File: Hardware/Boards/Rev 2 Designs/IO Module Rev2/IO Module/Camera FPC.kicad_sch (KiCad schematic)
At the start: 25 parts, among them J5 Cam FPC, U23 SN65DPHY440SS

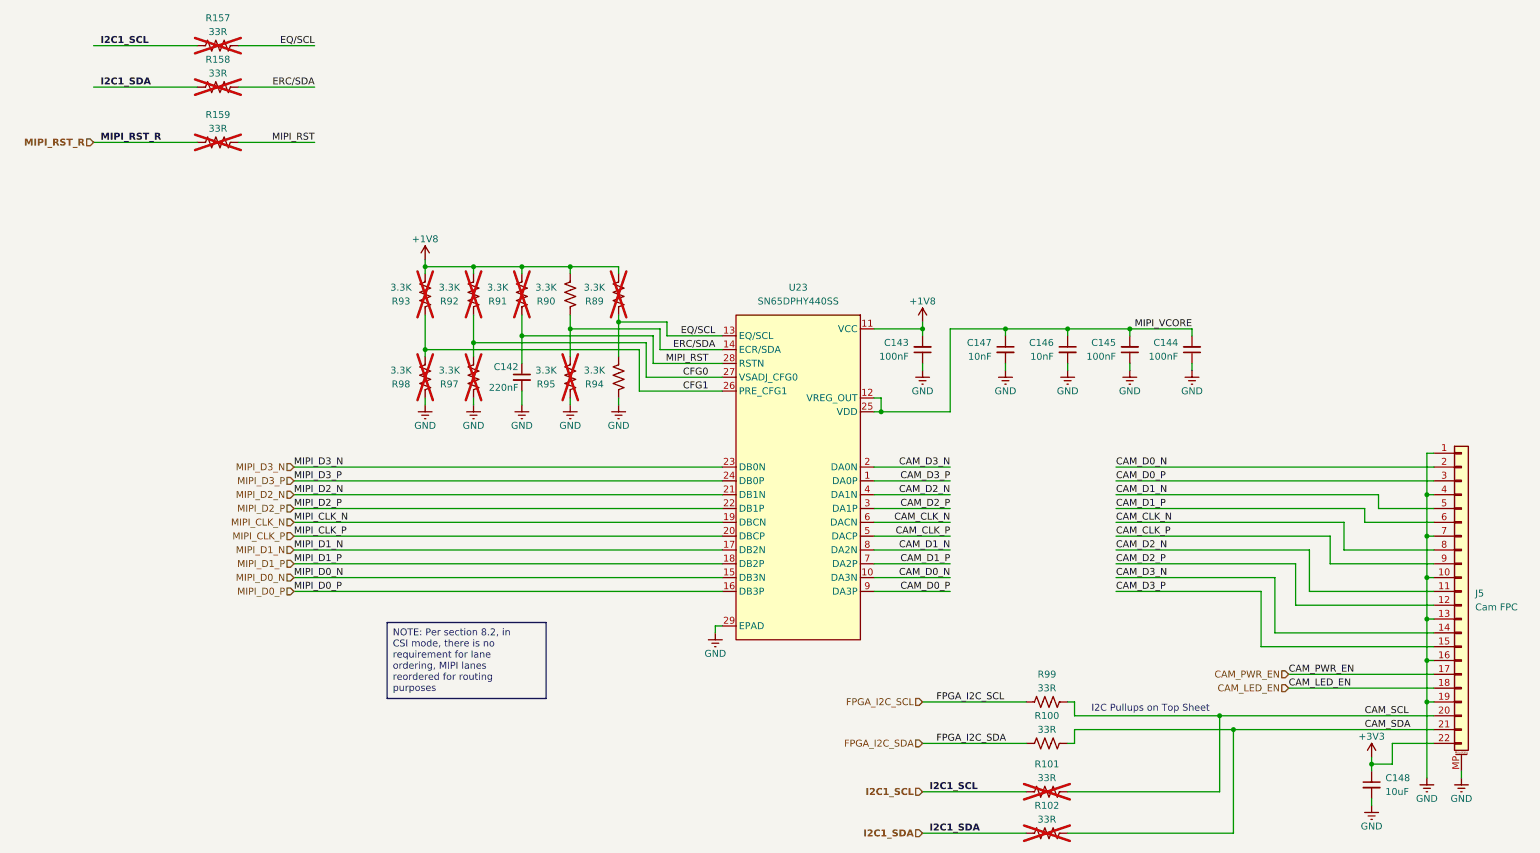
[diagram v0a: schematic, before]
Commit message: Rev 2 IO module complete
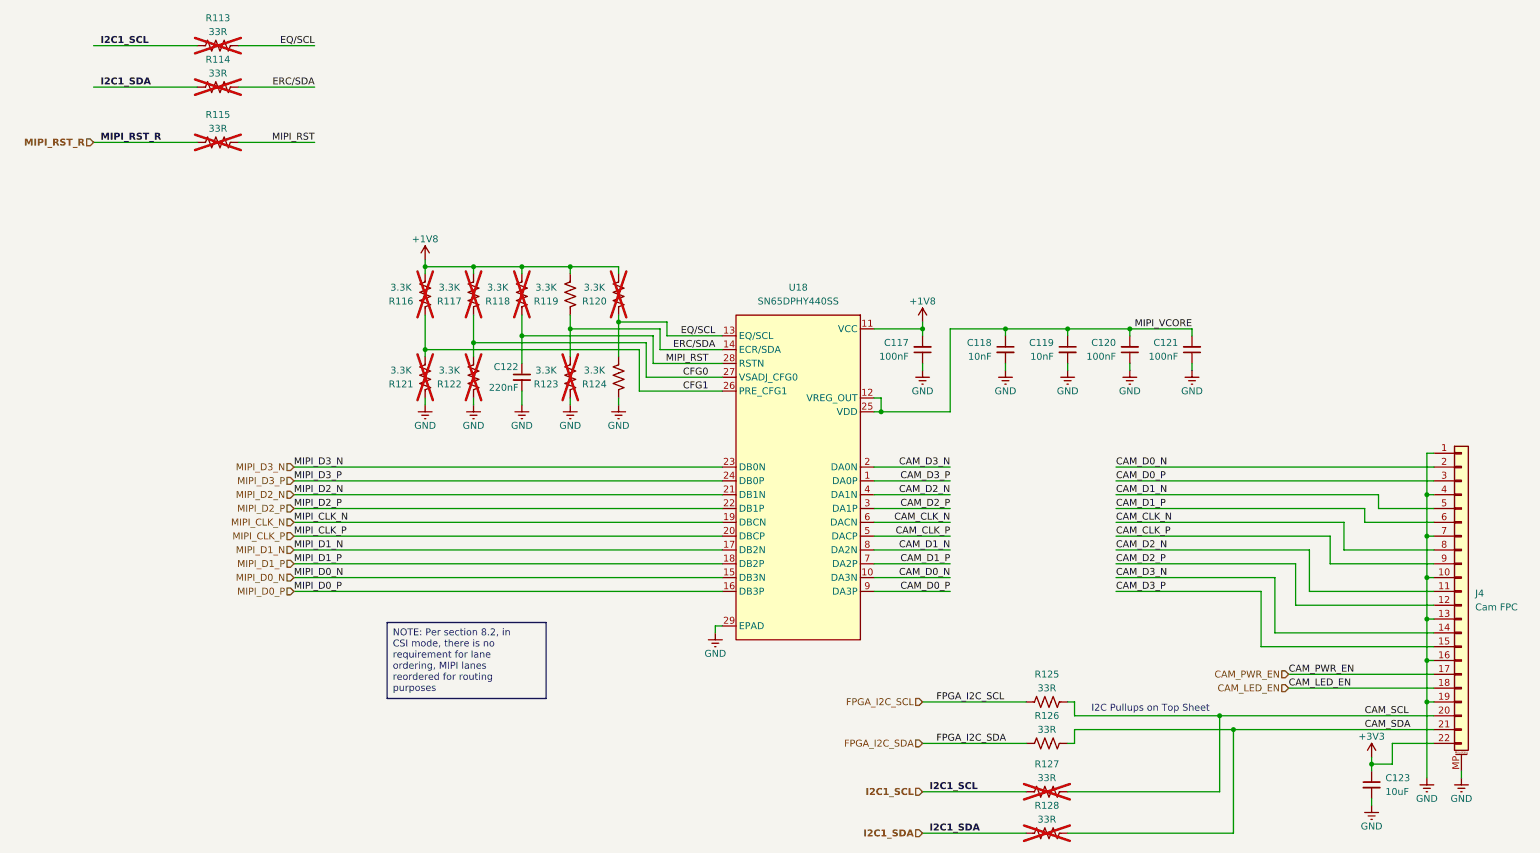
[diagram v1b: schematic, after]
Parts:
- U18: renamed from U23; footprint Package_DFN_QFN:QFN-28-1EP_3x6mm_P0.5mm_EP1.7x4.75mm -> IO_Module:RHR28_TEX-L
- renumbered C143 to C117, C147 to C118, C146 to C119, C145 to C120, C144 to C121, C142 to C122, C148 to C123, J5 to J4, R157 to R113, R158 to R114, R159 to R115, R93 to R116, R92 to R117, R91 to R118, R90 to R119, R89 to R120, R98 to R121, R97 to R122, R95 to R123, R94 to R124, R99 to R125, R100 to R126, R101 to R127, R102 to R128
